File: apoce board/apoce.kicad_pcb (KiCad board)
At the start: 2 copper layers, 6 parts, among them J6 Screw_Terminal_01x02, U1 4N35, U2 4N35

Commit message: Etape 1 pour le placement routage
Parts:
- removed J6: Screw_Terminal_01x02, Connector_Phoenix_MSTB:PhoenixContact_MSTBA_2,5_2-G_1x02_P5.00mm_Horizontal
- added D1: Vert Alim, LED_THT:LED_D5.0mm, F.Cu at (99.5, 104.0)
- added D10: LedModeJN-Bleu, LED_THT:LED_D5.0mm, F.Cu at (138.9, 132.7)
- added D11: LedModeSolCAV-Orange, LED_THT:LED_D5.0mm, F.Cu at (108.9, 140.2)
- added D12: LedModeSolAuto-Rouge, LED_THT:LED_D5.0mm, F.Cu at (116.4, 140.2)
- added D13: LedArmV-Blanc, LED_THT:LED_D5.0mm, F.Cu at (123.9, 140.2)
- added D2: Red, LED_THT:LED_D5.0mm, F.Cu at (116.4, 125.1)
- added D3: Jaune, LED_THT:LED_D5.0mm, F.Cu at (123.9, 125.1)
- added D4: LED-CA1-Vert, LED_THT:LED_D5.0mm, F.Cu at (131.4, 125.1)
- added D5: LED-CA2-Vert, LED_THT:LED_D5.0mm, F.Cu at (138.9, 125.1)
- added D6: LED-V-Vert, LED_THT:LED_D5.0mm, F.Cu at (108.9, 132.7)
- added D7: LED-X-Vert, LED_THT:LED_D5.0mm, F.Cu at (116.4, 132.7)
- added D8: Rouge, LED_THT:LED_D5.0mm, F.Cu at (123.9, 132.7)
- added D9: Jaune, LED_THT:LED_D5.0mm, F.Cu at (131.4, 132.7)
- added J1: Test Soleil, TerminalBlock:TerminalBlock_Xinya_XY308-2.54-3P_1x03_P2.54mm_Horizontal, F.Cu at (108.9, 156.7)
- added J2: Solaire, TerminalBlock_Phoenix:TerminalBlock_Phoenix_MKDS-1,5-2-5.08_1x02_P5.08mm_Horizontal, F.Cu at (29.0, 32.8)
- added J3: Test J/N, TerminalBlock:TerminalBlock_Xinya_XY308-2.54-3P_1x03_P2.54mm_Horizontal, F.Cu at (108.9, 165.2)
- added J4: Jour/Nuit, TerminalBlock:TerminalBlock_bornier-2_P5.08mm, F.Cu at (141.5, 26.0)
- added J5: Relais, TerminalBlock:TerminalBlock_Xinya_XY308-2.54-6P_1x06_P2.54mm_Horizontal, F.Cu at (108.9, 148.1)
- added R1: 1,5K, Resistor_THT:R_Axial_DIN0207_L6.3mm_D2.5mm_P10.16mm_Horizontal, F.Cu at (99.9, 84.5)
- added R10: 1,5K, Resistor_THT:R_Axial_DIN0207_L6.3mm_D2.5mm_P10.16mm_Horizontal, F.Cu at (82.4, 155.8)
- added R11: 1,5K, Resistor_THT:R_Axial_DIN0207_L6.3mm_D2.5mm_P10.16mm_Horizontal, F.Cu at (82.4, 159.8)
- added R12: 1,5K, Resistor_THT:R_Axial_DIN0207_L6.3mm_D2.5mm_P10.16mm_Horizontal, F.Cu at (82.4, 163.8)
- added R13: 1,5K, Resistor_THT:R_Axial_DIN0207_L6.3mm_D2.5mm_P10.16mm_Horizontal, F.Cu at (82.4, 167.9)
- added R2: 470, Resistor_THT:R_Axial_DIN0207_L6.3mm_D2.5mm_P10.16mm_Horizontal, F.Cu at (82.4, 127.4)
- added R3: 10K, Resistor_THT:R_Axial_DIN0207_L6.3mm_D2.5mm_P10.16mm_Horizontal, F.Cu at (82.4, 131.4)
- added R4: 1,5K, Resistor_THT:R_Axial_DIN0207_L6.3mm_D2.5mm_P10.16mm_Horizontal, F.Cu at (82.4, 135.5)
- added R5: 1,5K, Resistor_THT:R_Axial_DIN0207_L6.3mm_D2.5mm_P10.16mm_Horizontal, F.Cu at (184.3, 103.5)
- added R6: 1,5K, Resistor_THT:R_Axial_DIN0207_L6.3mm_D2.5mm_P10.16mm_Horizontal, F.Cu at (82.4, 139.6)
- added R7: 1,5K, Resistor_THT:R_Axial_DIN0207_L6.3mm_D2.5mm_P10.16mm_Horizontal, F.Cu at (82.4, 143.6)
- added R8: 470, Resistor_THT:R_Axial_DIN0207_L6.3mm_D2.5mm_P10.16mm_Horizontal, F.Cu at (82.4, 147.7)
- added R9: 10K, Resistor_THT:R_Axial_DIN0207_L6.3mm_D2.5mm_P10.16mm_Horizontal, F.Cu at (82.4, 151.7)
- added SW1: ButModeJN, TerminalBlock_Phoenix:TerminalBlock_Phoenix_MKDS-1,5-2-5.08_1x02_P5.08mm_Horizontal, F.Cu at (32.5, 183.8)
- added SW2: ButModeSolCAV, TerminalBlock_Phoenix:TerminalBlock_Phoenix_MKDS-1,5-2-5.08_1x02_P5.08mm_Horizontal, F.Cu at (57.0, 183.8)
- added SW3: ButModeSolAuto, TerminalBlock_Phoenix:TerminalBlock_Phoenix_MKDS-1,5-2-5.08_1x02_P5.08mm_Horizontal, F.Cu at (82.0, 183.8)
- added SW4: ButArmV, TerminalBlock_Phoenix:TerminalBlock_Phoenix_MKDS-1,5-2-5.08_1x02_P5.08mm_Horizontal, F.Cu at (106.0, 184.8)
- U1, U2: footprint Package_DIP:DIP-6_W7.62mm -> Package_DIP:DIP-6_W7.62mm_LongPads
- moved A1 148.8 mm to (215.8, 111.3)
- moved U2 77.2 mm to (211.7, 62.5)
- moved PS1 52.4 mm to (65.8, 31.5)
- moved U1 31.0 mm to (119.2, 60.5)
- moved PS2 9.39 mm to (168.3, 31.0)
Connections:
- A1 pad 20: unconnected-(A1-A1-Pad20) -> /X

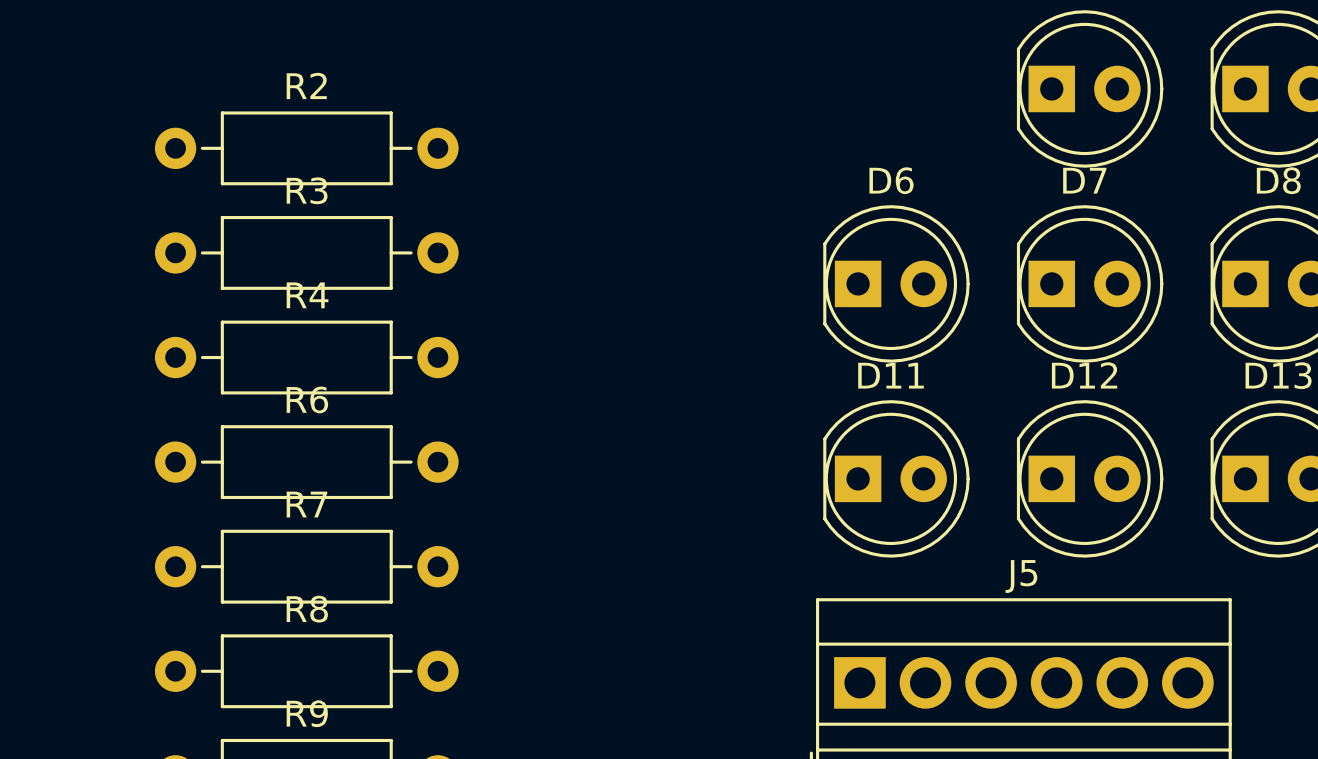
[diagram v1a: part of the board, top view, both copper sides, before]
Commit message: On a séparer les compteurs  Led de forcage
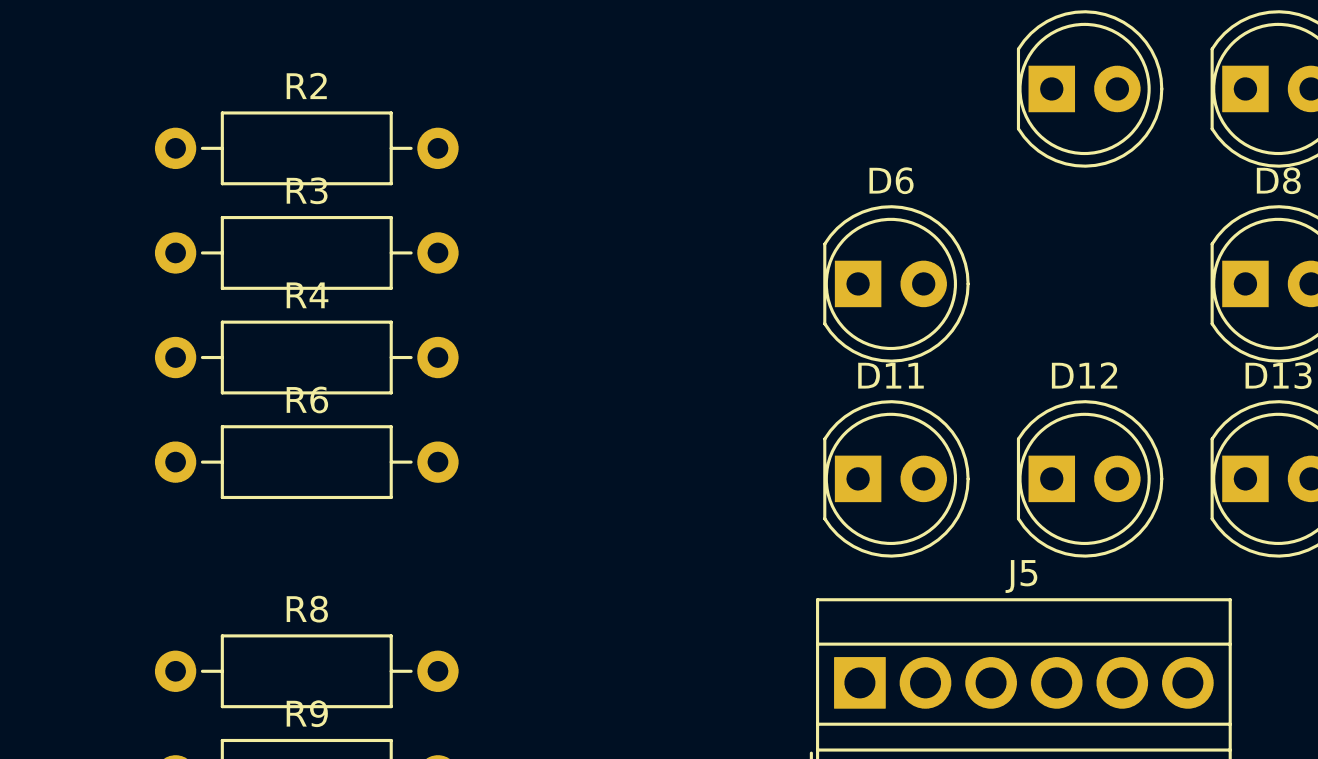
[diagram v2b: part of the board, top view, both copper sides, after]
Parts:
- removed D7: LED-X-Vert, LED_THT:LED_D5.0mm
- removed R7: 1,5K, Resistor_THT:R_Axial_DIN0207_L6.3mm_D2.5mm_P10.16mm_Horizontal
- D11: value LedModeSolCAV-Orange -> LedModeSol-Orange
- D12: value LedModeSolAuto-Rouge -> LedModeAuto-Rouge
- SW2: value ButModeSolCAV -> ButModeSol
- SW3: value ButModeSolAuto -> ButModeAuto
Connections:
- A1 pad 20: /X -> unconnected-(A1-A1-Pad20)
- J5 pad 5: /X -> unconnected-(J5-Pin_5-Pad5)
